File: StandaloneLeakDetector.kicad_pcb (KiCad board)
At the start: 2 copper layers, 32.5 x 34.5 mm, 16 parts, among them J1 TSW-102-07-L-S, J2 TSW-102-07-L-S, J3 Header, U1 QS6J11TR

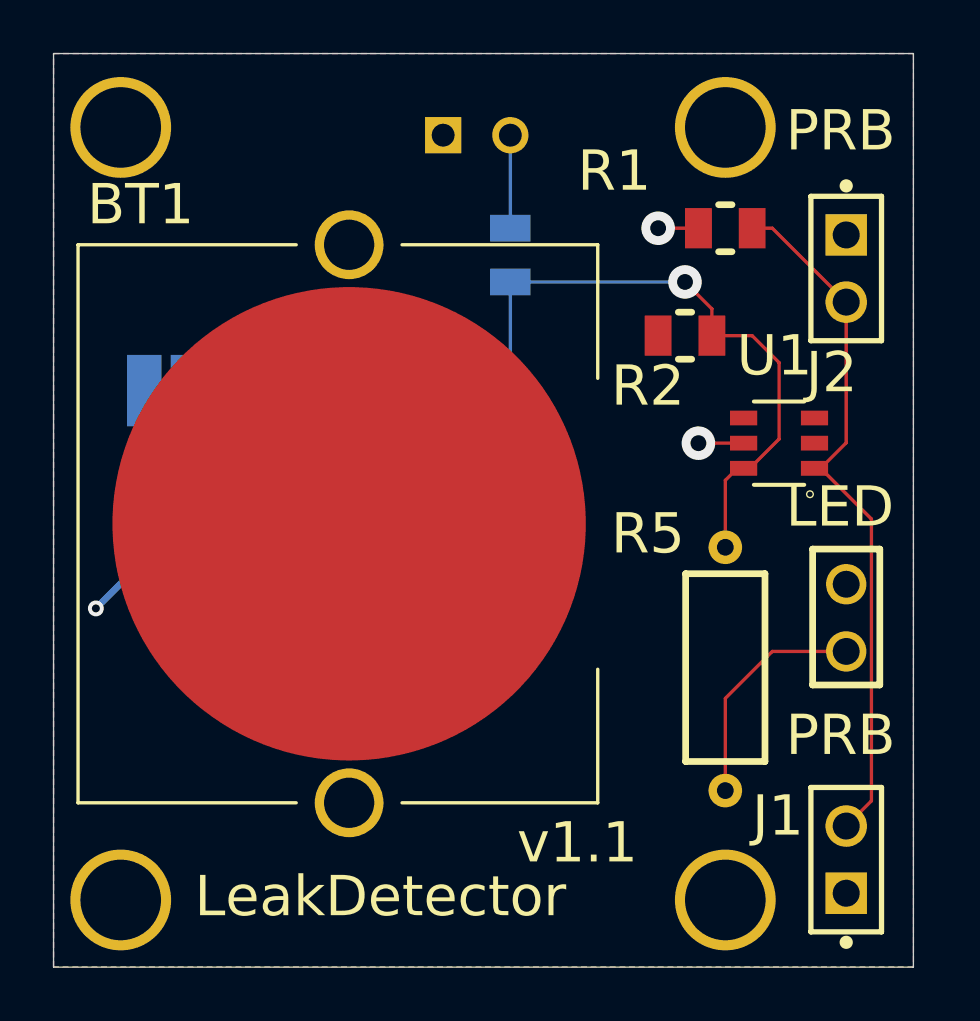
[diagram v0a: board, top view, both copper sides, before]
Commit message: Fix footprint associations
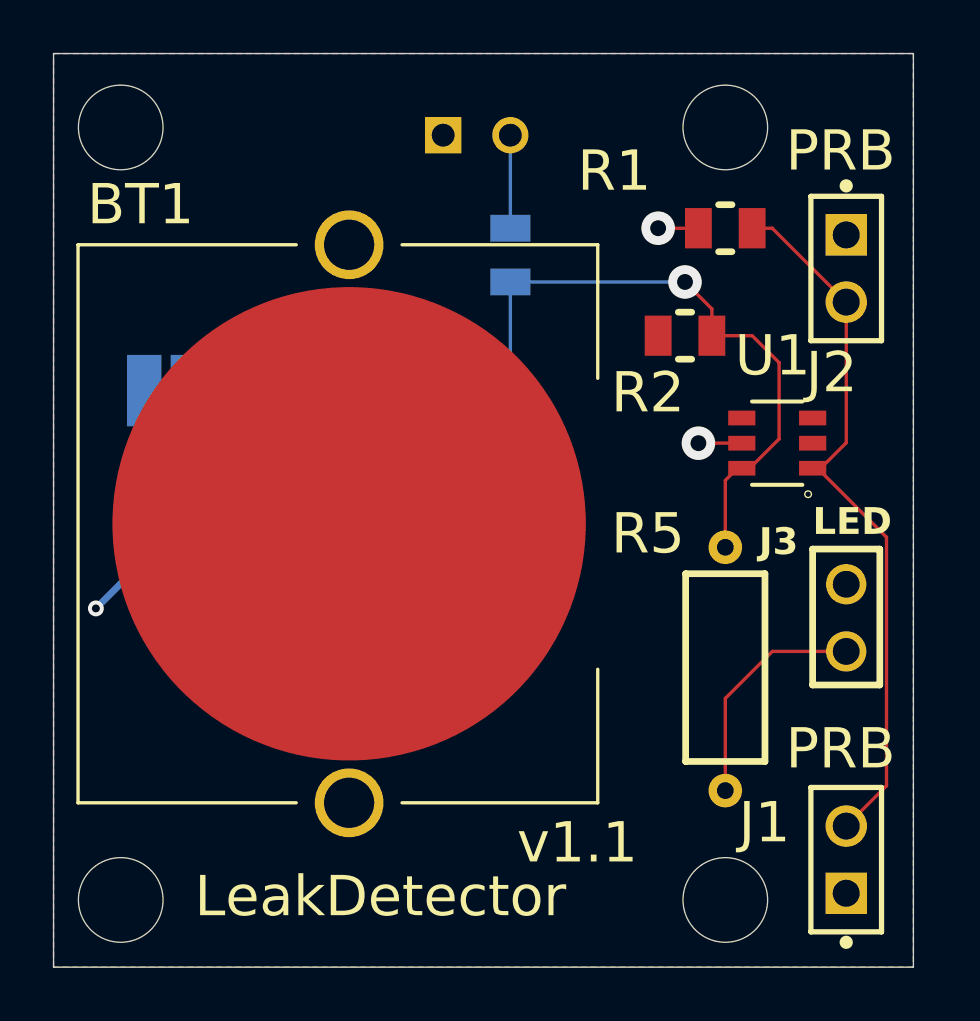
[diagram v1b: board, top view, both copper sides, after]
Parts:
- removed ? (x4): , AltiumImport:
- added G***: LOGO, AltiumImport:LOGO, B.Cu at (149.4, 108.3)
- added REF**: MountingHole_3.2mm_M3, AltiumImport:MountingHole_3.2mm_M3, F.Cu at (134.8, 90.5)
- added REF**: MountingHole_3.2mm_M3, AltiumImport:MountingHole_3.2mm_M3, F.Cu at (157.6, 119.7)
- added REF**: MountingHole_3.2mm_M3, AltiumImport:MountingHole_3.2mm_M3, F.Cu at (157.6, 90.5)
- added REF**: MountingHole_3.2mm_M3, AltiumImport:MountingHole_3.2mm_M3, F.Cu at (134.8, 119.7)
- moved U1 0.07 mm to (159.6, 102.5)
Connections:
- net 3V3 renamed /3V3
- net LEAK_IN renamed /LEAK_IN
- net LEAK_OUT renamed /LEAK_OUT
- net NetD1_2 renamed Net-(D1-Pad2)
- net NetD2_2 renamed Net-(D2-Pad2)
- net NetJ3_1 renamed Net-(J3-Pad1)
- U1 pad 2: (no net) -> unconnected-(U1-Pad2)
- U1 pad 3: (no net) -> unconnected-(U1-Pad3)
- U1 pad 4: (no net) -> unconnected-(U1-Pad4)
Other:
- rule pad_to_mask_clearance: 0 -> 0.05
